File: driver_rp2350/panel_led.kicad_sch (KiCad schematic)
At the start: 342 parts

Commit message: Worked on modifications for converting rp2350 design to 18x18 array.
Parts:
- R10, R11, R12, R13, R14, R15, R16, R17, R18, R19, R20, R21, R22, R23, R24, R25, R9: footprint (none) -> Resistor_SMD:R_0201_0603Metric
- R8: footprint panel_custom:JST_SH_BM04B-SRSS-TB_1x04-1MP_P1.00mm_Vertical -> Resistor_SMD:R_0201_0603Metric
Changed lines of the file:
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@@
 			)
 		)
-		(property "Footprint" ""
+		(property "Footprint" "Resistor_SMD:R_0201_0603Metric"
 			(at 82.042 53.34 90)
 			(effects
@@
 			)
 		)
-		(property "Footprint" ""
+		(property "Footprint" "Resistor_SMD:R_0201_0603Metric"
 			(at 64.262 53.34 90)
 			(effects
@@
 			)
 		)
-		(property "Footprint" ""
+		(property "Footprint" "Resistor_SMD:R_0201_0603Metric"
 			(at 153.162 53.34 90)
 			(effects
@@
 			)
 		)
-		(property "Footprint" ""
+		(property "Footprint" "Resistor_SMD:R_0201_0603Metric"
 			(at 277.622 53.34 90)
 			(effects
@@
 			)
 		)
-		(property "Footprint" ""
+		(property "Footprint" "Resistor_SMD:R_0201_0603Metric"
 			(at 259.842 53.34 90)
 			(effects
@@
 			)
 		)
-		(property "Footprint" ""
+		(property "Footprint" "Resistor_SMD:R_0201_0603Metric"
 			(at 206.502 53.34 90)
 			(effects
@@
 			)
 		)
-		(property "Footprint" ""
+		(property "Footprint" "Resistor_SMD:R_0201_0603Metric"
 			(at 224.282 53.34 90)
 			(effects
@@
 			)
 		)
-		(property "Footprint" ""
+		(property "Footprint" "Resistor_SMD:R_0201_0603Metric"
 			(at 117.602 53.34 90)
 			(effects
@@
 			)
 		)
-		(property "Footprint" ""
+		(property "Footprint" "Resistor_SMD:R_0201_0603Metric"
 			(at 170.942 53.34 90)
 			(effects
@@
 			)
 		)
-		(property "Footprint" ""
+		(property "Footprint" "Resistor_SMD:R_0201_0603Metric"
 			(at 330.962 53.34 90)
 			(effects
@@
 			)
 		)
-		(property "Footprint" "panel_custom:JST_SH_BM04B-SRSS-TB_1x04-1MP_P1.00mm_Vertical"
+		(property "Footprint" "Resistor_SMD:R_0201_0603Metric"
 			(at 28.702 53.34 90)
 			(effects
@@
 			)
 		)
-		(property "Footprint" ""
+		(property "Footprint" "Resistor_SMD:R_0201_0603Metric"
 			(at 188.722 53.34 90)
 			(effects
@@
 			)
 		)
-		(property "Footprint" ""
+		(property "Footprint" "Resistor_SMD:R_0201_0603Metric"
 			(at 99.822 53.34 90)
 			(effects
@@
 			)
 		)
-		(property "Footprint" ""
+		(property "Footprint" "Resistor_SMD:R_0201_0603Metric"
 			(at 46.482 53.34 90)
 			(effects
@@
 			)
 		)
-		(property "Footprint" ""
+		(property "Footprint" "Resistor_SMD:R_0201_0603Metric"
 			(at 242.062 53.34 90)
 			(effects
@@
 			)
 		)
-		(property "Footprint" ""
+		(property "Footprint" "Resistor_SMD:R_0201_0603Metric"
 			(at 295.402 53.34 90)
 			(effects
@@
 			)
 		)
-		(property "Footprint" ""
+		(property "Footprint" "Resistor_SMD:R_0201_0603Metric"
 			(at 313.182 53.34 90)
 			(effects
@@
 			)
 		)
-		(property "Footprint" ""
+		(property "Footprint" "Resistor_SMD:R_0201_0603Metric"
 			(at 135.382 53.34 90)
 			(effects

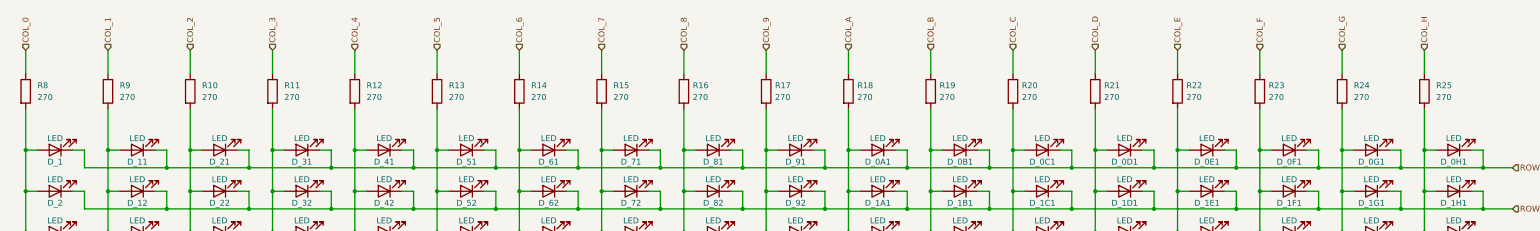
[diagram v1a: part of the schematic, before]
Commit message: Modified for rp2354.
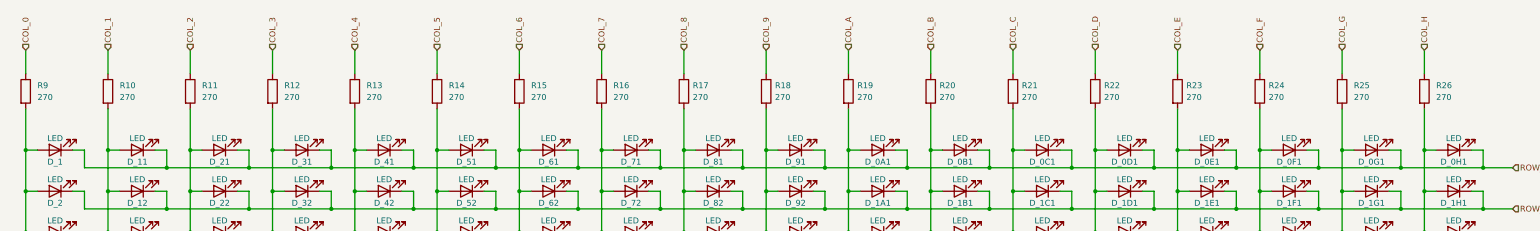
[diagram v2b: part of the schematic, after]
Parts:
- renumbered R9 to R10, R10 to R11, R11 to R12, R12 to R13, R13 to R14, R14 to R15, R15 to R16, R16 to R17, R17 to R18, R18 to R19, R19 to R20, R20 to R21, R21 to R22, R22 to R23, R23 to R24, R24 to R25, R25 to R26, R8 to R9
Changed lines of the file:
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@@
 		(dnp no)
 		(fields_autoplaced yes)
-		(property "Reference" "R11"
+		(property "Reference" "R12"
 			(at 86.36 52.0699 0)
 			(effects
@@
 			(project "panel"
 				(path "/1e634561-32a0-4ffa-9d4f-e93f355464d5/9e6027a1-8475-463d-b347-a287726616e8"
-					(reference "R11")
+					(reference "R12")
 					(unit 1)
 				)
@@
 		(dnp no)
 		(fields_autoplaced yes)
-		(property "Reference" "R10"
+		(property "Reference" "R11"
 			(at 68.58 52.0699 0)
 			(effects
@@
 			(project "panel"
 				(path "/1e634561-32a0-4ffa-9d4f-e93f355464d5/9e6027a1-8475-463d-b347-a287726616e8"
-					(reference "R10")
+					(reference "R11")
 					(unit 1)
 				)
@@
 		(dnp no)
 		(fields_autoplaced yes)
-		(property "Reference" "R15"
+		(property "Reference" "R16"
 			(at 157.48 52.0699 0)
 			(effects
@@
 			(project "panel"
 				(path "/1e634561-32a0-4ffa-9d4f-e93f355464d5/9e6027a1-8475-463d-b347-a287726616e8"
-					(reference "R15")
+					(reference "R16")
 					(unit 1)
 				)
@@
 		(dnp no)
 		(fields_autoplaced yes)
-		(property "Reference" "R22"
+		(property "Reference" "R23"
 			(at 281.305 52.0699 0)
 			(effects
@@
 			(project "panel"
 				(path "/1e634561-32a0-4ffa-9d4f-e93f355464d5/9e6027a1-8475-463d-b347-a287726616e8"
-					(reference "R22")
+					(reference "R23")
 					(unit 1)
 				)
@@
 		(dnp no)
 		(fields_autoplaced yes)
-		(property "Reference" "R21"
+		(property "Reference" "R22"
 			(at 263.525 52.0699 0)
 			(effects
@@
 			(project "panel"
 				(path "/1e634561-32a0-4ffa-9d4f-e93f355464d5/9e6027a1-8475-463d-b347-a287726616e8"
-					(reference "R21")
+					(reference "R22")
 					(unit 1)
 				)
@@
 		(dnp no)
 		(fields_autoplaced yes)
-		(property "Reference" "R18"
+		(property "Reference" "R19"
 			(at 210.185 52.0699 0)
 			(effects
@@
 			(project "panel"
 				(path "/1e634561-32a0-4ffa-9d4f-e93f355464d5/9e6027a1-8475-463d-b347-a287726616e8"
-					(reference "R18")
+					(reference "R19")
 					(unit 1)
 				)
@@
 		(dnp no)
 		(fields_autoplaced yes)
-		(property "Reference" "R19"
+		(property "Reference" "R20"
 			(at 227.965 52.0699 0)
 			(effects
@@
 			(project "panel"
 				(path "/1e634561-32a0-4ffa-9d4f-e93f355464d5/9e6027a1-8475-463d-b347-a287726616e8"
-					(reference "R19")
+					(reference "R20")
 					(unit 1)
 				)
@@
 		(dnp no)
 		(fields_autoplaced yes)
-		(property "Reference" "R13"
+		(property "Reference" "R14"
 			(at 121.92 52.0699 0)
 			(effects
@@
 			(project "panel"
 				(path "/1e634561-32a0-4ffa-9d4f-e93f355464d5/9e6027a1-8475-463d-b347-a287726616e8"
-					(reference "R13")
+					(reference "R14")
 					(unit 1)
 				)
@@
 		(dnp no)
 		(fields_autoplaced yes)
-		(property "Reference" "R16"
+		(property "Reference" "R17"
 			(at 174.625 52.0699 0)
 			(effects
@@
 			(project "panel"
 				(path "/1e634561-32a0-4ffa-9d4f-e93f355464d5/9e6027a1-8475-463d-b347-a287726616e8"
-					(reference "R16")
+					(reference "R17")
 					(unit 1)
 				)
@@
 		(dnp no)
 		(fields_autoplaced yes)
-		(property "Reference" "R25"
+		(property "Reference" "R26"
 			(at 335.28 52.0699 0)
 			(effects
@@
 			(project "driver_rp2350"
 				(path "/1e634561-32a0-4ffa-9d4f-e93f355464d5/9e6027a1-8475-463d-b347-a287726616e8"
-					(reference "R25")
+					(reference "R26")
 					(unit 1)
 				)
@@
 		(dnp no)
 		(fields_autoplaced yes)
-		(property "Reference" "R8"
+		(property "Reference" "R9"
 			(at 33.02 52.0699 0)
 			(effects
@@
 			(project "panel"
 				(path "/1e634561-32a0-4ffa-9d4f-e93f355464d5/9e6027a1-8475-463d-b347-a287726616e8"
-					(reference "R8")
+					(reference "R9")
 					(unit 1)
 				)
@@
 		(dnp no)
 		(fields_autoplaced yes)
-		(property "Reference" "R17"
+		(property "Reference" "R18"
 			(at 192.405 52.0699 0)
 			(effects
@@
 			(project "panel"
 				(path "/1e634561-32a0-4ffa-9d4f-e93f355464d5/9e6027a1-8475-463d-b347-a287726616e8"
-					(reference "R17")
+					(reference "R18")
 					(unit 1)
 				)
@@
 		(dnp no)
 		(fields_autoplaced yes)
-		(property "Reference" "R12"
+		(property "Reference" "R13"
 			(at 104.14 52.0699 0)
 			(effects
@@
 			(project "panel"
 				(path "/1e634561-32a0-4ffa-9d4f-e93f355464d5/9e6027a1-8475-463d-b347-a287726616e8"
-					(reference "R12")
+					(reference "R13")
 					(unit 1)
 				)
@@
 		(dnp no)
 		(fields_autoplaced yes)
-		(property "Reference" "R9"
+		(property "Reference" "R10"
 			(at 50.8 52.0699 0)
 			(effects
@@
 			(project "panel"
 				(path "/1e634561-32a0-4ffa-9d4f-e93f355464d5/9e6027a1-8475-463d-b347-a287726616e8"
-					(reference "R9")
+					(reference "R10")
 					(unit 1)
 				)
@@
 		(dnp no)
 		(fields_autoplaced yes)
-		(property "Reference" "R20"
+		(property "Reference" "R21"
 			(at 245.745 52.0699 0)
 			(effects
@@
 			(project "panel"
 				(path "/1e634561-32a0-4ffa-9d4f-e93f355464d5/9e6027a1-8475-463d-b347-a287726616e8"
-					(reference "R20")
+					(reference "R21")
 					(unit 1)
 				)
@@
 		(dnp no)
 		(fields_autoplaced yes)
-		(property "Reference" "R23"
+		(property "Reference" "R24"
 			(at 299.085 52.0699 0)
 			(effects
@@
 			(project "panel"
 				(path "/1e634561-32a0-4ffa-9d4f-e93f355464d5/9e6027a1-8475-463d-b347-a287726616e8"
-					(reference "R23")
+					(reference "R24")
 					(unit 1)
 				)
@@
 		(dnp no)
 		(fields_autoplaced yes)
-		(property "Reference" "R24"
+		(property "Reference" "R25"
 			(at 317.5 52.0699 0)
 			(effects
@@
 			(project "driver_rp2350"
 				(path "/1e634561-32a0-4ffa-9d4f-e93f355464d5/9e6027a1-8475-463d-b347-a287726616e8"
-					(reference "R24")
+					(reference "R25")
 					(unit 1)
 				)
@@
 		(dnp no)
 		(fields_autoplaced yes)
-		(property "Reference" "R14"
+		(property "Reference" "R15"
 			(at 139.7 52.0699 0)
 			(effects
@@
 			(project "panel"
 				(path "/1e634561-32a0-4ffa-9d4f-e93f355464d5/9e6027a1-8475-463d-b347-a287726616e8"
-					(reference "R14")
+					(reference "R15")
 					(unit 1)
 				)
